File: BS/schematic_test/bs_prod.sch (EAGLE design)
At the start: 20 parts, among them U1 ATMEGA328P_PDIP, U2 RFM69HW, Y1 16MHz

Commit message: BS schematic prod test add
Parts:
- added C2: (no value), SparkFun-Capacitors:CAP_POLC
- C1: value 10uF -> 0.1uF; device SparkFun-Capacitors:47UF-50V-20%(ELECT) -> SparkFun-Capacitors:CAP1206
- F1: value 500мА -> 500mA
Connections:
- new net N$16: C1.1, U1.AREF
- net 3.3V: now also C2.+; no longer C1.+
- net GND: now also C1.2, C2.-; no longer C1.-, U1.AREF
- net GPS_RX: now also U1.PD3(INT1); no longer U1.PD4(XCK/T0)
- net GPS_TX: now also U1.PD4(XCK/T0); no longer U1.PD3(INT1)
- net N$12: now also U1.PC0(ADC0); no longer U1.PB1(OC1A)
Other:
- moved on the sheet: C5, R3
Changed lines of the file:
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@@
 <setting verticaltext="up"/>
 </settings>
-<grid distance="0.1" unitdist="inch" unit="inch" style="lines" multiple="1" display="no" altdistance="0.01" altunitdist="inch" altunit="inch"/>
+<grid distance="0.1" unitdist="inch" unit="inch" style="lines" multiple="1" display="yes" altdistance="0.01" altunitdist="inch" altunit="inch"/>
 <layers>
 <layer number="1" name="Top" color="4" fill="1" visible="no" active="no"/>
@@
 <part name="SUPPLY1" library="SparkFun-Aesthetics" deviceset="3.3V" device=""/>
 <part name="SUPPLY2" library="SparkFun-Aesthetics" deviceset="5V" device=""/>
-<part name="GND1" library="SparkFun-Aesthetics" deviceset="GND" device=""/>
 <part name="C3" library="SparkFun-Capacitors" deviceset="CAP" device="1206" value="20pF"/>
 <part name="C4" library="SparkFun-Capacitors" deviceset="CAP" device="1206" value="20pF"/>
 <part name="GND2" library="SparkFun-Aesthetics" deviceset="GND" device=""/>
-<part name="C5" library="SparkFun-Capacitors" deviceset="CAP" device="1206" value="0.1uF"/>
 <part name="GND3" library="SparkFun-Aesthetics" deviceset="GND" device=""/>
 <part name="C6" library="SparkFun-Capacitors" deviceset="CAP" device="1206" value="0.1uF"/>
@@
 <part name="SMA" library="con-coax" deviceset="BU-SMC-V" device=""/>
 <part name="GND6" library="SparkFun-Aesthetics" deviceset="GND" device=""/>
-<part name="C1" library="SparkFun-Capacitors" deviceset="47UF-50V-20%(ELECT)" device="" value="10uF"/>
 <part name="JP2" library="SparkFun-Connectors" deviceset="M04" device="PTH"/>
 <part name="GND7" library="SparkFun-Aesthetics" deviceset="GND" device=""/>
 <part name="SUPPLY6" library="SparkFun-Aesthetics" deviceset="3.3V" device=""/>
-<part name="F1" library="fuse" deviceset="TE5" device="" value="500мА"/>
+<part name="F1" library="fuse" deviceset="TE5" device="" value="500mA"/>
 <part name="S1" library="switch-tact" deviceset="DTS-3" device=""/>
 <part name="GND8" library="SparkFun-Aesthetics" deviceset="GND" device=""/>
@@
 <part name="LED2" library="SparkFun-LED" deviceset="LED" device="1206"/>
 <part name="GND9" library="SparkFun-Aesthetics" deviceset="GND" device=""/>
+<part name="C2" library="SparkFun-Capacitors" deviceset="CAP_POL" device="C"/>
+<part name="C1" library="SparkFun-Capacitors" deviceset="CAP" device="1206" value="0.1uF"/>
+<part name="GND1" library="SparkFun-Aesthetics" deviceset="GND" device=""/>
+<part name="C5" library="SparkFun-Capacitors" deviceset="CAP" device="1206" value="0.1uF"/>
+<part name="SUPPLY7" library="SparkFun-Aesthetics" deviceset="3.3V" device=""/>
+<part name="GND10" library="SparkFun-Aesthetics" deviceset="GND" device=""/>
 </parts>
 <sheets>
@@
 <instance part="SUPPLY1" gate="G$1" x="15.24" y="152.4"/>
 <instance part="SUPPLY2" gate="G$1" x="40.64" y="68.58"/>
-<instance part="GND1" gate="1" x="15.24" y="127"/>
 <instance part="C3" gate="G$1" x="22.86" y="106.68" smashed="yes">
 <attribute name="NAME" x="19.304" y="109.347" size="1.778" layer="95"/>
@@
 </instance>
 <instance part="GND2" gate="1" x="25.4" y="86.36"/>
-<instance part="C5" gate="G$1" x="22.86" y="137.16" smashed="yes">
-<attribute name="NAME" x="23.876" y="139.827" size="1.778" layer="95"/>
-<attribute name="VALUE" x="23.876" y="135.001" size="1.778" layer="96"/>
-</instance>
 <instance part="GND3" gate="1" x="48.26" y="48.26"/>
 <instance part="C6" gate="G$1" x="40.64" y="35.56" smashed="yes">
@@
 </instance>
 <instance part="GND6" gate="1" x="165.1" y="88.9"/>
-<instance part="C1" gate="G$1" x="101.6" y="43.18"/>
 <instance part="JP2" gate="G$1" x="139.7" y="43.18"/>
 <instance part="GND7" gate="1" x="149.86" y="35.56"/>
@@
 <instance part="S1" gate="G$1" x="27.94" y="154.94"/>
 <instance part="GND8" gate="1" x="27.94" y="165.1" rot="R180"/>
-<instance part="R3" gate="G$1" x="88.9" y="104.14"/>
+<instance part="R3" gate="G$1" x="96.52" y="124.46" rot="R270"/>
 <instance part="LED2" gate="G$1" x="96.52" y="101.6"/>
 <instance part="GND9" gate="1" x="96.52" y="91.44"/>
+<instance part="C2" gate="G$1" x="101.6" y="43.18"/>
+<instance part="C1" gate="G$1" x="12.7" y="124.46" smashed="yes">
+<attribute name="NAME" x="8.382" y="127.127" size="1.778" layer="95"/>
+<attribute name="VALUE" x="5.334" y="122.301" size="1.778" layer="96"/>
+</instance>
+<instance part="GND1" gate="1" x="12.7" y="116.84"/>
+<instance part="C5" gate="G$1" x="99.06" y="71.12" smashed="yes" rot="MR0">
+<attribute name="NAME" x="103.378" y="73.787" size="1.778" layer="95" rot="MR0"/>
+<attribute name="VALUE" x="106.426" y="68.961" size="1.778" layer="96" rot="MR0"/>
+</instance>
+<instance part="SUPPLY7" gate="G$1" x="99.06" y="78.74"/>
+<instance part="GND10" gate="1" x="99.06" y="63.5"/>
 </instances>
 <busses>
@@
 <net name="3.3V" class="0">
 <segment>
-<pinref part="U1" gate="G$1" pin="AVCC"/>
-<pinref part="U1" gate="G$1" pin="VCC"/>
-<wire x1="30.48" y1="142.24" x2="30.48" y2="139.7" width="0.1524" layer="91"/>
-<wire x1="30.48" y1="142.24" x2="22.86" y2="142.24" width="0.1524" layer="91"/>
-<junction x="30.48" y="142.24"/>
 <pinref part="SUPPLY1" gate="G$1" pin="3.3V"/>
-<wire x1="22.86" y1="142.24" x2="15.24" y2="142.24" width="0.1524" layer="91"/>
 <wire x1="15.24" y1="142.24" x2="15.24" y2="147.32" width="0.1524" layer="91"/>
 <pinref part="R1" gate="G$1" pin="1"/>
 <junction x="15.24" y="147.32"/>
 <wire x1="15.24" y1="147.32" x2="15.24" y2="152.4" width="0.1524" layer="91"/>
-<pinref part="C5" gate="G$1" pin="1"/>
-<junction x="22.86" y="142.24"/>
+<pinref part="U1" gate="G$1" pin="VCC"/>
+<pinref part="U1" gate="G$1" pin="AVCC"/>
+<wire x1="30.48" y1="142.24" x2="30.48" y2="139.7" width="0.1524" layer="91"/>
+<wire x1="30.48" y1="142.24" x2="15.24" y2="142.24" width="0.1524" layer="91"/>
+<junction x="30.48" y="142.24"/>
 </segment>
 <segment>
@@
 <pinref part="R2" gate="G$1" pin="1"/>
 <wire x1="101.6" y1="48.26" x2="106.68" y2="48.26" width="0.1524" layer="91"/>
-<pinref part="C1" gate="G$1" pin="+"/>
+<pinref part="C2" gate="G$1" pin="+"/>
 </segment>
 <segment>
@@
 <pinref part="SUPPLY6" gate="G$1" pin="3.3V"/>
 </segment>
+<segment>
+<pinref part="C5" gate="G$1" pin="1"/>
+<pinref part="SUPPLY7" gate="G$1" pin="3.3V"/>
+<wire x1="99.06" y1="76.2" x2="99.06" y2="78.74" width="0.1524" layer="91"/>
+</segment>
 </net>
 <net name="GND" class="0">
-<segment>
-<pinref part="U1" gate="G$1" pin="AREF"/>
-<wire x1="30.48" y1="132.08" x2="22.86" y2="132.08" width="0.1524" layer="91"/>
-<pinref part="GND1" gate="1" pin="GND"/>
-<wire x1="22.86" y1="132.08" x2="15.24" y2="132.08" width="0.1524" layer="91"/>
-<wire x1="15.24" y1="132.08" x2="15.24" y2="129.54" width="0.1524" layer="91"/>
-<pinref part="C5" gate="G$1" pin="2"/>
-<wire x1="22.86" y1="134.62" x2="22.86" y2="132.08" width="0.1524" layer="91"/>
-<junction x="22.86" y="132.08"/>
-</segment>
 <segment>
 <pinref part="C3" gate="G$1" pin="2"/>
@@
 <pinref part="LED1" gate="G$1" pin="C"/>
 <wire x1="116.84" y1="38.1" x2="101.6" y2="38.1" width="0.1524" layer="91"/>
-<pinref part="C1" gate="G$1" pin="-"/>
+<pinref part="C2" gate="G$1" pin="-"/>
 <wire x1="101.6" y1="38.1" x2="88.9" y2="38.1" width="0.1524" layer="91"/>
 <junction x="101.6" y="38.1"/>
@@
 <pinref part="GND9" gate="1" pin="GND"/>
 </segment>
+<segment>
+<pinref part="C1" gate="G$1" pin="2"/>
+<pinref part="GND1" gate="1" pin="GND"/>
+<wire x1="12.7" y1="121.92" x2="12.7" y2="119.38" width="0.1524" layer="91"/>
+</segment>
+<segment>
+<pinref part="GND10" gate="1" pin="GND"/>
+<pinref part="C5" gate="G$1" pin="2"/>
+<wire x1="99.06" y1="66.04" x2="99.06" y2="68.58" width="0.1524" layer="91"/>
+</segment>
 </net>
 <net name="N$6" class="0">
@@
 </segment>
 <segment>
+<pinref part="U1" gate="G$1" pin="PD4(XCK/T0)"/>
+<wire x1="78.74" y1="114.3" x2="83.82" y2="114.3" width="0.1524" layer="91"/>
+<label x="78.74" y="114.3" size="1.778" layer="95"/>
+</segment>
+</net>
+<net name="GPS_RX" class="0">
+<segment>
+<pinref part="JP2" gate="G$1" pin="2"/>
+<wire x1="144.78" y1="43.18" x2="149.86" y2="43.18" width="0.1524" layer="91"/>
+<label x="144.78" y="43.18" size="1.778" layer="95"/>
+</segment>
+<segment>
 <pinref part="U1" gate="G$1" pin="PD3(INT1)"/>
 <wire x1="78.74" y1="116.84" x2="83.82" y2="116.84" width="0.1524" layer="91"/>
 <label x="78.74" y="116.84" size="1.778" layer="95"/>
-</segment>
-</net>
-<net name="GPS_RX" class="0">
-<segment>
-<pinref part="JP2" gate="G$1" pin="2"/>
-<wire x1="144.78" y1="43.18" x2="149.86" y2="43.18" width="0.1524" layer="91"/>
-<label x="144.78" y="43.18" size="1.778" layer="95"/>
-</segment>
-<segment>
-<pinref part="U1" gate="G$1" pin="PD4(XCK/T0)"/>
-<wire x1="78.74" y1="114.3" x2="83.82" y2="114.3" width="0.1524" layer="91"/>
-<label x="78.74" y="114.3" size="1.778" layer="95"/>
 </segment>
 </net>
@@
 </segment>
 </net>
-<net name="N$12" class="0">
-<segment>
-<pinref part="U1" gate="G$1" pin="PB1(OC1A)"/>
-<wire x1="78.74" y1="99.06" x2="83.82" y2="99.06" width="0.1524" layer="91"/>
-<pinref part="R3" gate="G$1" pin="1"/>
-<wire x1="83.82" y1="99.06" x2="83.82" y2="104.14" width="0.1524" layer="91"/>
-</segment>
-</net>
 <net name="N$13" class="0">
 <segment>
 <pinref part="R3" gate="G$1" pin="2"/>
 <pinref part="LED2" gate="G$1" pin="A"/>
-<wire x1="93.98" y1="104.14" x2="96.52" y2="104.14" width="0.1524" layer="91"/>
-</segment>
-</net>
+<wire x1="96.52" y1="119.38" x2="96.52" y2="104.14" width="0.1524" layer="91"/>
+</segment>
+</net>
+<net name="N$12" class="0">
+<segment>
+<pinref part="R3" gate="G$1" pin="1"/>
+<wire x1="96.52" y1="129.54" x2="96.52" y2="147.32" width="0.1524" layer="91"/>
+<pinref part="U1" gate="G$1" pin="PC0(ADC0)"/>
+<wire x1="96.52" y1="147.32" x2="78.74" y2="147.32" width="0.1524" layer="91"/>
+</segment>
+</net>
+<net name="N$16" class="0">
+<segment>
+<pinref part="U1" gate="G$1" pin="AREF"/>
+<wire x1="30.48" y1="132.08" x2="12.7" y2="132.08" width="0.1524" layer="91"/>
+<pinref part="C1" gate="G$1" pin="1"/>
+<wire x1="12.7" y1="132.08" x2="12.7" y2="129.54" width="0.1524" layer="91"/>
+</segment>
+</net>

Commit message: BS schematic prod
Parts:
- removed S1: DTS-3, switch-tact:DTS-3
- added C8, C9: 0.1uF, SparkFun-Capacitors:CAP1206
- added JP3: (no value), SparkFun-Connectors:M06SIP
- added JP4: (no value), SparkFun-Connectors:M05PTH
- added RESET: DTSM-3, switch-tact:DTSM-3
- added U$1: UBLOX, myGps:UBLOX
- C2: value (none) -> 10uF
- renumbered LED1 to PWR
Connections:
- new net A0: JP3.4, U1.PC5(ADC5/SCL)
- new net A1: JP3.3, U1.PC4(ADC4/SDA)
- new net A2: JP3.2, U1.PC3(ADC3)
- new net A3: JP3.1, U1.PC2(ADC2)
- new net D5: JP4.1, U1.PD5(T1)
- new net D6: JP4.2, U1.PD6(AIN0)
- new net D7: JP4.3, U1.PD7(AIN1)
- net 3.3V: now also C8.1, C9.1, JP3.5, JP4.4
- net GND: now also C8.2, C9.2, JP3.6, JP4.5, RESET.2; no longer S1.2
- net RST: now also RESET.1; no longer S1.1

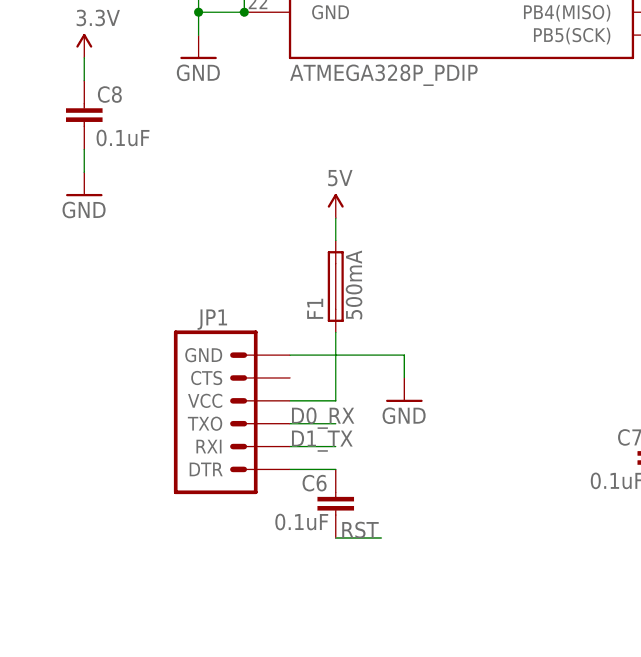
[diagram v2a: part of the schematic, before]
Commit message: add polygon to BS schematic
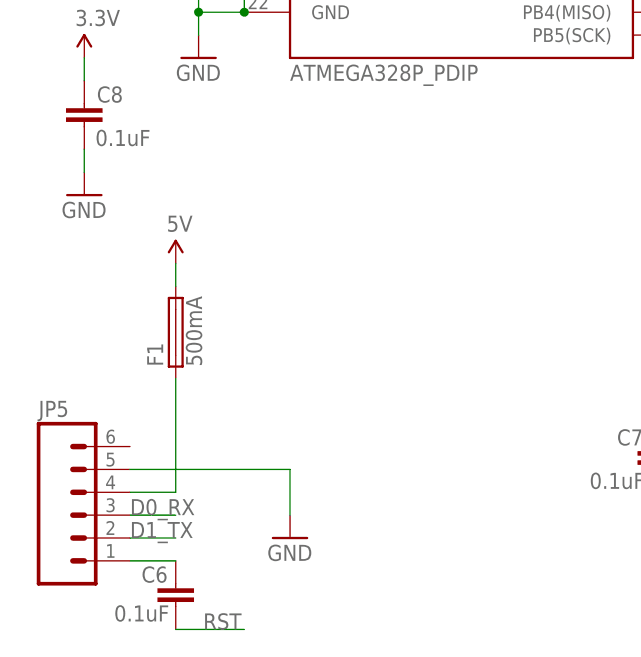
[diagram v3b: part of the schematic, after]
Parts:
- removed JP1: (no value), SparkFun-Connectors:ARDUINO_SERIAL_PROGRAMPTH
- added JP5: (no value), SparkFun-Connectors:M06SIP
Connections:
- net D0_RX: now also JP5.3; no longer JP1.TXO
- net D1_TX: now also JP5.2; no longer JP1.RXI
- net GND: now also JP5.5; no longer JP1.GND
- net N$11: now also JP5.1; no longer JP1.DTR
- net N$9: now also JP5.4; no longer JP1.VCC
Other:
- moved on the sheet: C6, F1
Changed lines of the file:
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@@
 <part name="LR-3.3" library="lm1117" deviceset="LM1117IMPX-*" device="" technology="3.3"/>
 <part name="FRAME1" library="frames" deviceset="A4L-LOC" device=""/>
-<part name="JP1" library="SparkFun-Connectors" deviceset="ARDUINO_SERIAL_PROGRAM" device="PTH"/>
 <part name="R1" library="SparkFun-Resistors" deviceset="RESISTOR" device="1206" value="10k"/>
 <part name="Y1" library="SparkFun-FreqCtrl" deviceset="CRYSTAL" device="SMD" value="16MHz"/>
@@
 <part name="SUPPLY9" library="SparkFun-Aesthetics" deviceset="3.3V" device=""/>
 <part name="GND12" library="SparkFun-Aesthetics" deviceset="GND" device=""/>
+<part name="JP5" library="SparkFun-Connectors" deviceset="M06" device="SIP"/>
 </parts>
 <sheets>
@@
 </instance>
 <instance part="FRAME1" gate="G$1" x="0" y="0"/>
-<instance part="JP1" gate="G$1" x="30.48" y="45.72"/>
 <instance part="R1" gate="G$1" x="20.32" y="147.32"/>
 <instance part="Y1" gate="G$1" x="25.4" y="114.3" smashed="yes" rot="R180">
@@
 <instance part="PWR" gate="G$1" x="116.84" y="43.18"/>
 <instance part="SUPPLY1" gate="G$1" x="15.24" y="152.4"/>
-<instance part="SUPPLY2" gate="G$1" x="40.64" y="68.58"/>
+<instance part="SUPPLY2" gate="G$1" x="22.86" y="63.5"/>
 <instance part="C3" gate="G$1" x="22.86" y="106.68" smashed="yes">
 <attribute name="NAME" x="19.304" y="109.347" size="1.778" layer="95"/>
@@
 </instance>
 <instance part="GND2" gate="1" x="25.4" y="86.36"/>
-<instance part="GND3" gate="1" x="48.26" y="48.26"/>
-<instance part="C6" gate="G$1" x="40.64" y="35.56" smashed="yes">
-<attribute name="NAME" x="36.83" y="38.227" size="1.778" layer="95"/>
-<attribute name="VALUE" x="33.782" y="33.909" size="1.778" layer="96"/>
+<instance part="GND3" gate="1" x="35.56" y="33.02"/>
+<instance part="C6" gate="G$1" x="22.86" y="25.4" smashed="yes">
+<attribute name="NAME" x="19.05" y="28.067" size="1.778" layer="95"/>
+<attribute name="VALUE" x="16.002" y="23.749" size="1.778" layer="96"/>
 </instance>
 <instance part="SUPPLY3" gate="G$1" x="76.2" y="50.8"/>
@@
 <instance part="GND7" gate="1" x="149.86" y="35.56"/>
 <instance part="SUPPLY6" gate="G$1" x="149.86" y="50.8"/>
-<instance part="F1" gate="1" x="40.64" y="60.96" rot="R90"/>
+<instance part="F1" gate="1" x="22.86" y="55.88" rot="R90"/>
 <instance part="GND8" gate="1" x="27.94" y="165.1" rot="R180"/>
 <instance part="R3" gate="G$1" x="96.52" y="124.46" rot="R270"/>
@@
 <instance part="SUPPLY9" gate="G$1" x="182.88" y="78.74"/>
 <instance part="GND12" gate="1" x="182.88" y="63.5"/>
+<instance part="JP5" gate="G$1" x="12.7" y="35.56"/>
 </instances>
 <busses>
@@
 <segment>
 <pinref part="C6" gate="G$1" pin="2"/>
-<wire x1="40.64" y1="33.02" x2="45.72" y2="33.02" width="0.1524" layer="91"/>
-<label x="41.148" y="33.02" size="1.778" layer="95"/>
+<wire x1="22.86" y1="22.86" x2="30.48" y2="22.86" width="0.1524" layer="91"/>
+<label x="25.908" y="22.86" size="1.778" layer="95"/>
 </segment>
 </net>
@@
 </segment>
 <segment>
-<pinref part="JP1" gate="G$1" pin="GND"/>
-<wire x1="35.56" y1="53.34" x2="48.26" y2="53.34" width="0.1524" layer="91"/>
-<wire x1="48.26" y1="53.34" x2="48.26" y2="50.8" width="0.1524" layer="91"/>
-<pinref part="GND3" gate="1" pin="GND"/>
-</segment>
-<segment>
 <pinref part="LR-3.3" gate="G$1" pin="GND"/>
 <wire x1="88.9" y1="40.64" x2="88.9" y2="38.1" width="0.1524" layer="91"/>
@@
 <wire x1="182.88" y1="66.04" x2="182.88" y2="68.58" width="0.1524" layer="91"/>
 </segment>
+<segment>
+<pinref part="JP5" gate="G$1" pin="5"/>
+<wire x1="17.78" y1="40.64" x2="35.56" y2="40.64" width="0.1524" layer="91"/>
+<pinref part="GND3" gate="1" pin="GND"/>
+<wire x1="35.56" y1="40.64" x2="35.56" y2="35.56" width="0.1524" layer="91"/>
+</segment>
 </net>
 <net name="N$6" class="0">
@@
 <pinref part="SUPPLY2" gate="G$1" pin="5V"/>
 <pinref part="F1" gate="1" pin="2"/>
-<wire x1="40.64" y1="68.58" x2="40.64" y2="66.04" width="0.1524" layer="91"/>
+<wire x1="22.86" y1="63.5" x2="22.86" y2="60.96" width="0.1524" layer="91"/>
 </segment>
 </net>
 <net name="D0_RX" class="0">
-<segment>
-<pinref part="JP1" gate="G$1" pin="TXO"/>
-<wire x1="35.56" y1="45.72" x2="40.64" y2="45.72" width="0.1524" layer="91"/>
-<label x="35.56" y="45.72" size="1.778" layer="95"/>
-</segment>
 <segment>
 <pinref part="U1" gate="G$1" pin="PD0(RXD)"/>
@@
 <label x="78.74" y="124.46" size="1.778" layer="95"/>
 </segment>
+<segment>
+<pinref part="JP5" gate="G$1" pin="3"/>
+<wire x1="17.78" y1="35.56" x2="22.86" y2="35.56" width="0.1524" layer="91"/>
+<label x="17.78" y="35.56" size="1.778" layer="95"/>
+</segment>
 </net>
 <net name="D1_TX" class="0">
-<segment>
-<pinref part="JP1" gate="G$1" pin="RXI"/>
-<wire x1="35.56" y1="43.18" x2="40.64" y2="43.18" width="0.1524" layer="91"/>
-<label x="35.56" y="43.18" size="1.778" layer="95"/>
-</segment>
 <segment>
 <pinref part="U1" gate="G$1" pin="PD1(TXD)"/>
@@
 <label x="78.74" y="121.92" size="1.778" layer="95"/>
 </segment>
-</net>
-<net name="N$11" class="0">
-<segment>
-<pinref part="JP1" gate="G$1" pin="DTR"/>
-<pinref part="C6" gate="G$1" pin="1"/>
-<wire x1="35.56" y1="40.64" x2="40.64" y2="40.64" width="0.1524" layer="91"/>
+<segment>
+<pinref part="JP5" gate="G$1" pin="2"/>
+<wire x1="17.78" y1="33.02" x2="22.86" y2="33.02" width="0.1524" layer="91"/>
+<label x="17.78" y="33.02" size="1.778" layer="95"/>
 </segment>
 </net>
@@
 </segment>
 </net>
-<net name="N$9" class="0">
-<segment>
-<pinref part="JP1" gate="G$1" pin="VCC"/>
-<wire x1="35.56" y1="48.26" x2="40.64" y2="48.26" width="0.1524" layer="91"/>
-<pinref part="F1" gate="1" pin="1"/>
-<wire x1="40.64" y1="55.88" x2="40.64" y2="48.26" width="0.1524" layer="91"/>
-</segment>
-</net>
 <net name="N$13" class="0">
 <segment>
@@
 </segment>
 </net>
+<net name="N$11" class="0">
+<segment>
+<pinref part="JP5" gate="G$1" pin="1"/>
+<pinref part="C6" gate="G$1" pin="1"/>
+<wire x1="17.78" y1="30.48" x2="22.86" y2="30.48" width="0.1524" layer="91"/>
+</segment>
+</net>
+<net name="N$9" class="0">
+<segment>
+<pinref part="JP5" gate="G$1" pin="4"/>
+<wire x1="17.78" y1="38.1" x2="22.86" y2="38.1" width="0.1524" layer="91"/>
+<pinref part="F1" gate="1" pin="1"/>
+<wire x1="22.86" y1="38.1" x2="22.86" y2="50.8" width="0.1524" layer="91"/>
+</segment>
+</net>

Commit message: final BS schematic
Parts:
- C9: value 0.1uF -> 0.47uF
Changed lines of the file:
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@@
 <setting verticaltext="up"/>
 </settings>
-<grid distance="0.1" unitdist="inch" unit="inch" style="lines" multiple="1" display="yes" altdistance="0.01" altunitdist="inch" altunit="inch"/>
+<grid distance="0.1" unitdist="inch" unit="inch" style="lines" multiple="1" display="no" altdistance="0.01" altunitdist="inch" altunit="inch"/>
 <layers>
 <layer number="1" name="Top" color="4" fill="1" visible="no" active="no"/>
@@
 <part name="SUPPLY8" library="SparkFun-Aesthetics" deviceset="3.3V" device=""/>
 <part name="GND11" library="SparkFun-Aesthetics" deviceset="GND" device=""/>
-<part name="C9" library="SparkFun-Capacitors" deviceset="CAP" device="1206" value="0.1uF"/>
+<part name="C9" library="SparkFun-Capacitors" deviceset="CAP" device="1206" value="0.47uF"/>
 <part name="SUPPLY9" library="SparkFun-Aesthetics" deviceset="3.3V" device=""/>
 <part name="GND12" library="SparkFun-Aesthetics" deviceset="GND" device=""/>
